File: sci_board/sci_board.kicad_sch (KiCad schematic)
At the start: 5 parts

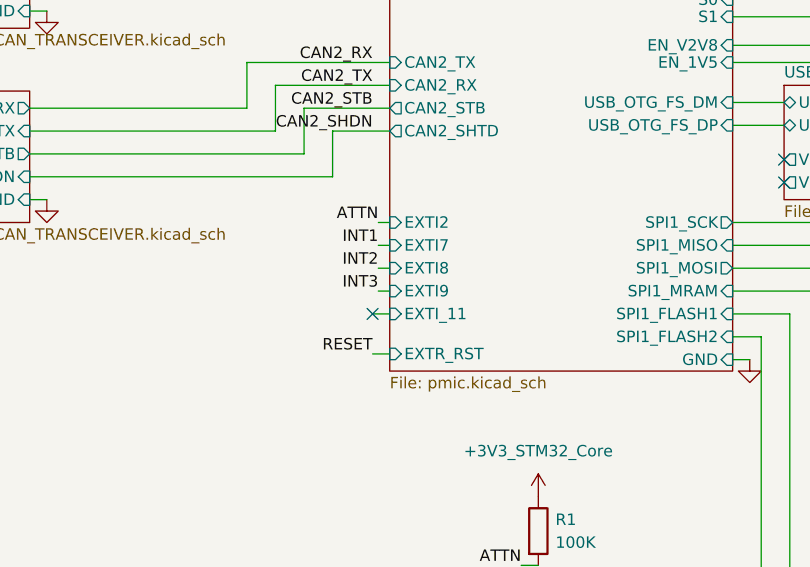
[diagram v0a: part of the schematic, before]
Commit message: add SPI CS and MISO pullups and terminations, remove WD from SCI
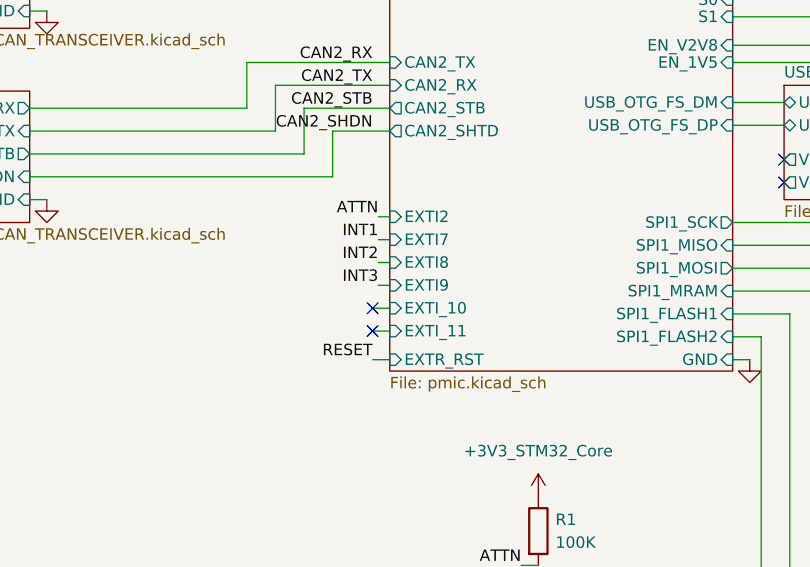
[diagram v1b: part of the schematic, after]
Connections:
- no-connect marks 37 -> 38
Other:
- sheet PMIC ports: added EXTI_10; removed none
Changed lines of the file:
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@@
 	)
 	(no_connect
+		(at 86.36 126.365)
+	)
+	(no_connect
 		(at 88.265 40.005)
 	)
 	(no_connect
-		(at 86.36 124.46)
+		(at 86.36 123.825)
 	)
 	(no_connect
@@
 	(wire
 		(pts
-			(xy 86.995 119.38) (xy 88.265 119.38)
+			(xy 86.995 118.745) (xy 88.265 118.745)
 		)
 		(stroke
@@
 	(wire
 		(pts
-			(xy 86.995 114.3) (xy 88.265 114.3)
+			(xy 86.995 113.665) (xy 88.265 113.665)
 		)
 		(stroke
@@
 	(wire
 		(pts
-			(xy 86.995 121.92) (xy 88.265 121.92)
+			(xy 86.995 121.285) (xy 88.265 121.285)
 		)
 		(stroke
@@
 	(wire
 		(pts
+			(xy 86.36 126.365) (xy 88.265 126.365)
+		)
+		(stroke
+			(width 0)
+			(type default)
+		)
+	)
+	(wire
+		(pts
 			(xy 48.26 88.265) (xy 88.265 88.265)
 		)
@@
 	(wire
 		(pts
-			(xy 86.36 124.46) (xy 88.265 124.46)
+			(xy 86.36 123.825) (xy 88.265 123.825)
 		)
 		(stroke
@@
 	(wire
 		(pts
-			(xy 86.36 128.905) (xy 88.265 128.905)
+			(xy 86.36 129.54) (xy 88.265 129.54)
 		)
 		(stroke
@@
 	(wire
 		(pts
-			(xy 86.995 116.84) (xy 88.265 116.84)
+			(xy 86.995 116.205) (xy 88.265 116.205)
 		)
 		(stroke
@@
 	)
 	(label "INT3"
-		(at 86.995 121.92 180)
+		(at 86.995 121.285 180)
 		(fields_autoplaced yes)
 		(effects
@@
 	)
 	(label "INT2"
-		(at 86.995 119.38 180)
+		(at 86.995 118.745 180)
 		(fields_autoplaced yes)
 		(effects
@@
 	)
 	(label "INT1"
-		(at 86.995 116.84 180)
+		(at 86.995 116.205 180)
 		(fields_autoplaced yes)
 		(effects
@@
 	)
 	(label "ATTN"
-		(at 86.995 114.3 180)
+		(at 86.995 113.665 180)
 		(fields_autoplaced yes)
 		(effects
@@
 	)
 	(label "RESET"
-		(at 86.36 128.905 180)
+		(at 86.36 129.54 180)
 		(fields_autoplaced yes)
 		(effects
@@
 		)
 		(pin "EXTI8" input
-			(at 88.265 119.38 180)
+			(at 88.265 118.745 180)
 			(effects
 				(font
@@
 		)
 		(pin "EXTI7" input
-			(at 88.265 116.84 180)
+			(at 88.265 116.205 180)
 			(effects
 				(font
@@
 		)
 		(pin "EXTI9" input
-			(at 88.265 121.92 180)
+			(at 88.265 121.285 180)
 			(effects
 				(font
@@
 		)
 		(pin "EXTR_RST" input
-			(at 88.265 128.905 180)
+			(at 88.265 129.54 180)
 			(effects
 				(font
@@
 		)
 		(pin "EXTI_11" input
-			(at 88.265 124.46 180)
+			(at 88.265 126.365 180)
 			(effects
 				(font
@@
 		)
 		(pin "EXTI2" input
-			(at 88.265 114.3 180)
+			(at 88.265 113.665 180)
 			(effects
 				(font
@@
 			(effects
 				(font
+					(size 1.27 1.27)
+				)
+				(justify left)
+			)
+		)
+		(pin "EXTI_10" input
+			(at 88.265 123.825 180)
+			(effects
+				(font

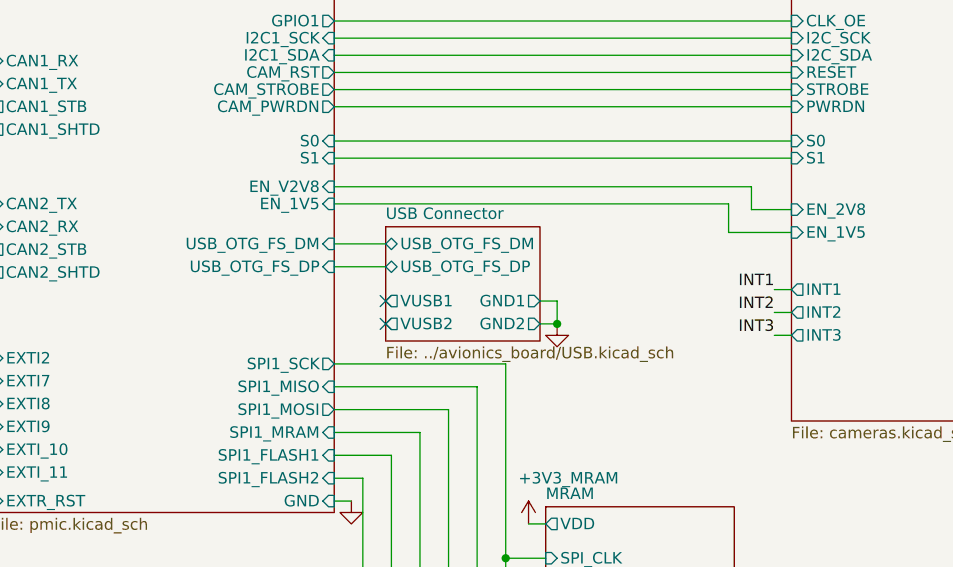
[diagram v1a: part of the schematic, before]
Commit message: tweaking SCI and AUX for production, using common sheets as much as possible
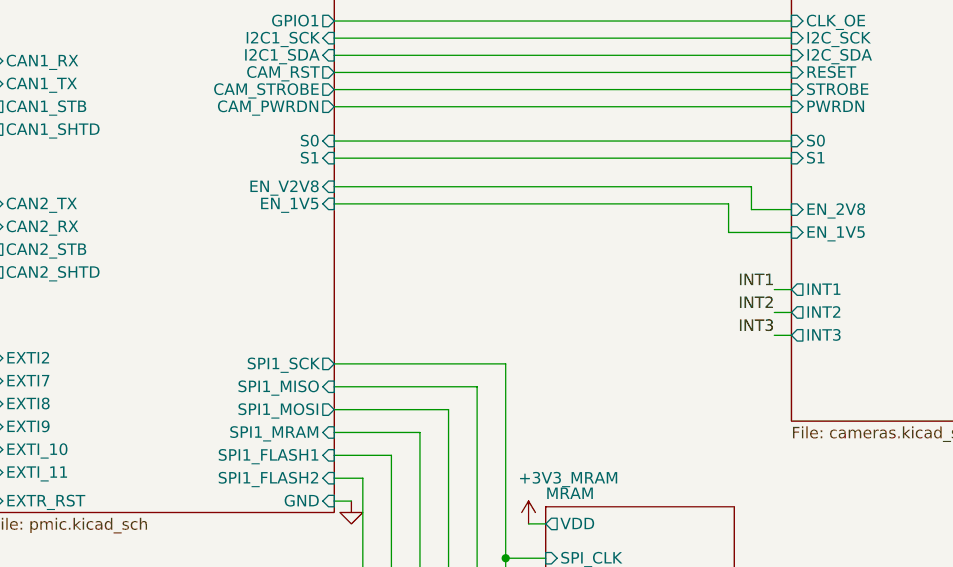
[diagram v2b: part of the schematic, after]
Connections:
- no-connect marks 38 -> 36
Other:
- removed sheet USB Connector
- sheet PMIC ports: added none; removed USB_OTG_FS_DM, USB_OTG_FS_DP
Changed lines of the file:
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@@
 	)
 	(junction
-		(at 151.13 109.855)
-		(diameter 0)
-		(color 0 0 0 0)
-	)
-	(junction
 		(at 142.24 138.43)
 		(diameter 0)
@@
 	)
 	(no_connect
-		(at 132.08 109.855)
-	)
-	(no_connect
 		(at 88.265 42.545)
 	)
@@
 	)
 	(no_connect
-		(at 132.08 107.315)
-	)
-	(no_connect
 		(at 266.7 47.625)
 	)
@@
 	(wire
 		(pts
-			(xy 149.225 107.315) (xy 151.13 107.315)
-		)
-		(stroke
-			(width 0)
-			(type default)
-		)
-	)
-	(wire
-		(pts
 			(xy 126.365 76.2) (xy 177.165 76.2)
 		)
@@
 	(wire
 		(pts
-			(xy 126.365 100.965) (xy 132.08 100.965)
-		)
-		(stroke
-			(width 0)
-			(type default)
-		)
-	)
-	(wire
-		(pts
 			(xy 139.065 165.735) (xy 149.86 165.735)
 		)
@@
 	(wire
 		(pts
-			(xy 149.225 109.855) (xy 151.13 109.855)
-		)
-		(stroke
-			(width 0)
-			(type default)
-		)
-	)
-	(wire
-		(pts
 			(xy 126.365 43.815) (xy 177.165 43.815)
 		)
@@
 	(wire
 		(pts
-			(xy 126.365 103.505) (xy 132.08 103.505)
-		)
-		(stroke
-			(width 0)
-			(type default)
-		)
-	)
-	(wire
-		(pts
 			(xy 22.225 90.805) (xy 24.765 90.805)
 		)
@@
 	(wire
 		(pts
-			(xy 151.13 107.315) (xy 151.13 109.855)
-		)
-		(stroke
-			(width 0)
-			(type default)
-		)
-	)
-	(wire
-		(pts
 			(xy 86.995 116.205) (xy 88.265 116.205)
 		)
@@
 		(dnp no)
 		(fields_autoplaced yes)
-		(property "Reference" "#PWR034"
+		(property "Reference" "#PWR033"
 			(at 174.625 198.12 0)
 			(effects
@@
 			(project "sci_board"
 				(path "/b4b2c88d-f6cd-4e60-862d-e21f68728580"
-					(reference "#PWR034")
+					(reference "#PWR033")
 					(unit 1)
 				)
@@
 		(dnp no)
 		(fields_autoplaced yes)
-		(property "Reference" "#PWR025"
+		(property "Reference" "#PWR024"
 			(at 213.995 125.095 0)
 			(effects
@@
 			(project "sci_board"
 				(path "/b4b2c88d-f6cd-4e60-862d-e21f68728580"
-					(reference "#PWR025")
+					(reference "#PWR024")
 					(unit 1)
 				)
@@
 	)
 	(symbol
-		(lib_id "power:GND")
-		(at 151.13 109.855 0)
-		(unit 1)
-		(exclude_from_sim no)
-		(in_bom yes)
-		(on_board yes)
-		(dnp no)
-		(fields_autoplaced yes)
-		(property "Reference" "#PWR023"
-			(at 151.13 116.205 0)
-			(effects
-				(font
-					(size 1.27 1.27)
-				)
-				(hide yes)
-			)
-		)
-		(property "Value" "GND"
-			(at 151.13 114.3 0)
-			(effects
-				(font
-					(size 1.27 1.27)
-				)
-				(hide yes)
-			)
-		)
-		(property "Footprint" ""
-			(at 151.13 109.855 0)
-			(effects
-				(font
-					(size 1.27 1.27)
-				)
-				(hide yes)
-			)
-		)
-		(property "Datasheet" ""
-			(at 151.13 109.855 0)
-			(effects
-				(font
-					(size 1.27 1.27)
-				)
-				(hide yes)
-			)
-		)
-		(property "Description" "Power symbol creates a global label with name \"GND\" , ground"
-			(at 151.13 109.855 0)
-			(effects
-				(font
-					(size 1.27 1.27)
-				)
-				(hide yes)
-			)
-		)
-		(pin "1"
-		)
-		(instances
-			(project "sci_board"
-				(path "/b4b2c88d-f6cd-4e60-862d-e21f68728580"
-					(reference "#PWR023")
-					(unit 1)
-				)
-			)
-		)
-	)
-	(symbol
 		(lib_id "power:PWR_FLAG")
 		(at 67.945 20.955 270)
@@
 		(dnp no)
 		(fields_autoplaced yes)
-		(property "Reference" "#PWR026"
+		(property "Reference" "#PWR025"
 			(at 128.27 135.89 0)
 			(effects
@@
 			(project "sci_board"
 				(path "/b4b2c88d-f6cd-4e60-862d-e21f68728580"
-					(reference "#PWR026")
+					(reference "#PWR025")
 					(unit 1)
 				)
@@
 		(on_board yes)
 		(dnp no)
-		(property "Reference" "#PWR027"
+		(property "Reference" "#PWR026"
 			(at 147.955 135.89 0)
 			(effects
@@
 			(project "sci_board"
 				(path "/b4b2c88d-f6cd-4e60-862d-e21f68728580"
-					(reference "#PWR027")
+					(reference "#PWR026")
 					(unit 1)
 				)
@@
 		(dnp no)
 		(fields_autoplaced yes)
-		(property "Reference" "#PWR024"
+		(property "Reference" "#PWR023"
 			(at 50.165 118.11 0)
 			(effects
@@
 			(project "sci_board"
 				(path "/b4b2c88d-f6cd-4e60-862d-e21f68728580"
-					(reference "#PWR024")
+					(reference "#PWR023")
 					(unit 1)
 				)
@@
 		(dnp no)
 		(fields_autoplaced yes)
-		(property "Reference" "#PWR029"
+		(property "Reference" "#PWR028"
 			(at 173.99 151.13 0)
 			(effects
@@
 			(project "sci_board"
 				(path "/b4b2c88d-f6cd-4e60-862d-e21f68728580"
-					(reference "#PWR029")
+					(reference "#PWR028")
 					(unit 1)
 				)
@@
 		(dnp no)
 		(fields_autoplaced yes)
-		(property "Reference" "#PWR031"
+		(property "Reference" "#PWR030"
 			(at 275.59 168.91 0)
 			(effects
@@
 			(project "sci_board"
 				(path "/b4b2c88d-f6cd-4e60-862d-e21f68728580"
-					(reference "#PWR031")
+					(reference "#PWR030")
 					(unit 1)
 				)
@@
 		(dnp no)
 		(fields_autoplaced yes)
-		(property "Reference" "#PWR032"
+		(property "Reference" "#PWR031"
 			(at 174.625 174.625 0)
 			(effects
@@
 			(project "sci_board"
 				(path "/b4b2c88d-f6cd-4e60-862d-e21f68728580"
-					(reference "#PWR032")
+					(reference "#PWR031")
 					(unit 1)
 				)
@@
 		(on_board yes)
 		(dnp no)
-		(property "Reference" "#PWR033"
+		(property "Reference" "#PWR032"
 			(at 147.32 184.15 0)
 			(effects
@@
 			(project "sci_board"
 				(path "/b4b2c88d-f6cd-4e60-862d-e21f68728580"
-					(reference "#PWR033")
+					(reference "#PWR032")
 					(unit 1)
 				)
@@
 		(on_board yes)
 		(dnp no)
-		(property "Reference" "#PWR030"
+		(property "Reference" "#PWR029"
 			(at 147.32 160.655 0)
 			(effects
@@
 			(project "sci_board"
 				(path "/b4b2c88d-f6cd-4e60-862d-e21f68728580"
-					(reference "#PWR030")
+					(reference "#PWR029")
 					(unit 1)
 				)
@@
 		(dnp no)
 		(fields_autoplaced yes)
-		(property "Reference" "#PWR028"
+		(property "Reference" "#PWR027"
 			(at 104.775 148.59 0)
 			(effects
@@
 			(project "sci_board"
 				(path "/b4b2c88d-f6cd-4e60-862d-e21f68728580"
-					(reference "#PWR028")
+					(reference "#PWR027")
 					(unit 1)
 				)
@@
 			)
 		)
-		(pin "USB_OTG_FS_DM" input
-			(at 126.365 100.965 0)
-			(effects
-				(font
-					(size 1.27 1.27)
-				)
-				(justify right)
-			)
-		)
-		(pin "USB_OTG_FS_DP" input
-			(at 126.365 103.505 0)
-			(effects
-				(font
-					(size 1.27 1.27)
-				)
-				(justify right)
-			)
-		)
 		(pin "DCMI_02" input
 			(at 126.365 49.53 0)
@@
 				)
 			)
-		)
-	)
-	(sheet
-		(at 132.08 99.06)
-		(size 17.145 12.7)
-		(fields_autoplaced yes)
-		(stroke
-			(width 0.1524)
-			(type solid)
-		)
-		(fill
-			(color 0 0 0 0.0000)
-		)
-		(property "Sheetname" "USB Connector"
-			(at 132.08 98.3484 0)
-			(effects
-				(font
-					(size 1.27 1.27)
-				)
-				(justify left bottom)
-			)
-		)
-		(property "Sheetfile" "../avionics_board/USB.kicad_sch"
-			(at 132.08 112.3446 0)
-			(effects
-				(font
-					(size 1.27 1.27)
-				)
-				(justify left top)
-			)
-		)
-		(pin "GND1" output
-			(at 149.225 107.315 0)
-			(effects
-				(font
-					(size 1.27 1.27)
-				)
-				(justify right)
-			)
-		)
-		(pin "USB_OTG_FS_DM" bidirectional
-			(at 132.08 100.965 180)
-			(effects
-				(font
-					(size 1.27 1.27)
-				)
-				(justify left)
-			)
-		)
-		(pin "VUSB1" output
-			(at 132.08 107.315 180)
-			(effects
-				(font
-					(size 1.27 1.27)
-				)
-				(justify left)
-			)
-		)
-		(pin "GND2" output
-			(at 149.225 109.855 0)
-			(effects
-				(font
-					(size 1.27 1.27)
-				)
-				(justify right)
-			)
-		)
-		(pin "VUSB2" output
-			(at 132.08 109.855 180)
-			(effects
-				(font
-					(size 1.27 1.27)
-				)
-				(justify left)
-			)
-		)
-		(pin "USB_OTG_FS_DP" bidirectional
-			(at 132.08 103.505 180)
-			(effects
-				(font
-					(size 1.27 1.27)
-				)
-				(justify left)
-			)
-		)
-		(instances
-			(project "sci_board"
-				(path "/b4b2c88d-f6cd-4e60-862d-e21f68728580"
-					(page "15")
-				)
-			)

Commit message: clenup BOM for SCI and AUX
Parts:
- R1: value 100K -> 330K
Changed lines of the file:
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@@
 			)
 		)
-		(property "Value" "100K"
+		(property "Value" "330K"
 			(at 106.68 149.8599 0)
 			(effects

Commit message: cleaning up bom: remove main camera port since it has not pullups and capacitors, correcting some errors in camera switch
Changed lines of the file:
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@@
+	)
+	(symbol
+		(lib_id "power:GND")
+		(at 141.605 19.05 0)
+		(mirror y)
+		(unit 1)
+		(exclude_from_sim no)
+		(in_bom yes)
+		(on_board yes)
+		(dnp no)
+		(fields_autoplaced yes)
+		(property "Reference" "#PWR02"
+			(at 141.605 25.4 0)
+			(effects
+				(font
+					(size 1.27 1.27)
+				)
+				(hide yes)
+			)
+		)
+		(property "Value" "GND"
+			(at 141.605 23.495 0)
+			(effects
+				(font
+					(size 1.27 1.27)
+				)
+				(hide yes)
+			)
+		)
+		(property "Footprint" ""
+			(at 141.605 19.05 0)
+			(effects
+				(font
+					(size 1.27 1.27)
+				)
+				(hide yes)
+			)
+		)
+		(property "Datasheet" ""
+			(at 141.605 19.05 0)
+			(effects
+				(font
+					(size 1.27 1.27)
+				)
+				(hide yes)
+			)
+		)
+		(property "Description" "Power symbol creates a global label with name \"GND\" , ground"
+			(at 141.605 19.05 0)
+			(effects
+				(font
+					(size 1.27 1.27)
+				)
+				(hide yes)
+			)
+		)
+		(pin "1"
+		)
+		(instances
+			(project "sci_board"
+				(path "/b4b2c88d-f6cd-4e60-862d-e21f68728580"
+					(reference "#PWR02")
+					(unit 1)
+				)
+			)
+		)
 	)
 	(symbol
@@
 	)
 	(symbol
+		(lib_id "power:PWR_FLAG")
+		(at 141.605 19.05 270)
+		(unit 1)
+		(exclude_from_sim no)
+		(in_bom yes)
+		(on_board yes)
+		(dnp no)
+		(fields_autoplaced yes)
+		(property "Reference" "#FLG02"
+			(at 143.51 19.05 0)
+			(effects
+				(font
+					(size 1.27 1.27)
+				)
+				(hide yes)
+			)
+		)
+		(property "Value" "PWR_FLAG"
+			(at 144.78 19.0499 90)
+			(effects
+				(font
+					(size 1.27 1.27)
+				)
+				(justify left)
+			)
+		)
+		(property "Footprint" ""
+			(at 141.605 19.05 0)
+			(effects
+				(font
+					(size 1.27 1.27)
+				)
+				(hide yes)
+			)
+		)
+		(property "Datasheet" "~"
+			(at 141.605 19.05 0)
+			(effects
+				(font
+					(size 1.27 1.27)
+				)
+				(hide yes)
+			)
+		)
+		(property "Description" "Special symbol for telling ERC where power comes from"
+			(at 141.605 19.05 0)
+			(effects
+				(font
+					(size 1.27 1.27)
+				)
+				(hide yes)
+			)
+		)
+		(pin "1"
+		)
+		(instances
+			(project "sci_board"
+				(path "/b4b2c88d-f6cd-4e60-862d-e21f68728580"
+					(reference "#FLG02")
+					(unit 1)
+				)
+			)
+		)
+	)
+	(symbol
 		(lib_id "power:GND")
 		(at 53.975 56.515 0)
@@
 				(path "/b4b2c88d-f6cd-4e60-862d-e21f68728580"
 					(reference "#PWR025")
-					(unit 1)
-				)
-			)
-		)
-	)
-	(symbol
-		(lib_id "power:PWR_FLAG")
-		(at 134.62 18.415 270)
-		(unit 1)
-		(exclude_from_sim no)
-		(in_bom yes)
-		(on_board yes)
-		(dnp no)
-		(fields_autoplaced yes)
-		(property "Reference" "#FLG02"
-			(at 136.525 18.415 0)
-			(effects
-				(font
-					(size 1.27 1.27)
-				)
-				(hide yes)
-			)
-		)
-		(property "Value" "PWR_FLAG"
-			(at 137.795 18.4149 90)
-			(effects
-				(font
-					(size 1.27 1.27)
-				)
-				(justify left)
-			)
-		)
-		(property "Footprint" ""
-			(at 134.62 18.415 0)
-			(effects
-				(font
-					(size 1.27 1.27)
-				)
-				(hide yes)
-			)
-		)
-		(property "Datasheet" "~"
-			(at 134.62 18.415 0)
-			(effects
-				(font
-					(size 1.27 1.27)
-				)
-				(hide yes)
-			)
-		)
-		(property "Description" "Special symbol for telling ERC where power comes from"
-			(at 134.62 18.415 0)
-			(effects
-				(font
-					(size 1.27 1.27)
-				)
-				(hide yes)
-			)
-		)
-		(pin "1"
-		)
-		(instances
-			(project "sci_board"
-				(path "/b4b2c88d-f6cd-4e60-862d-e21f68728580"
-					(reference "#FLG02")
 					(unit 1)
 				)
@@
 					(unit 1)
 				)
-			)
-		)
-	)
-	(symbol
-		(lib_id "power:GND")
-		(at 134.62 18.415 0)
-		(mirror y)
-		(unit 1)
-		(exclude_from_sim no)
-		(in_bom yes)
-		(on_board yes)
-		(dnp no)
-		(fields_autoplaced yes)
-		(property "Reference" "#PWR02"
-			(at 134.62 24.765 0)
-			(effects
-				(font
-					(size 1.27 1.27)
-				)
-				(hide yes)
-			)
-		)
-		(property "Value" "GND"
-			(at 134.62 22.86 0)
-			(effects
-				(font
-					(size 1.27 1.27)
-				)
-				(hide yes)
-			)
-		)
-		(property "Footprint" ""
-			(at 134.62 18.415 0)
-			(effects
-				(font
-					(size 1.27 1.27)
-				)
-				(hide yes)
-			)
-		)
-		(property "Datasheet" ""
-			(at 134.62 18.415 0)
-			(effects
-				(font
-					(size 1.27 1.27)
-				)
-				(hide yes)
-			)
-		)
-		(property "Description" "Power symbol creates a global label with name \"GND\" , ground"
-			(at 134.62 18.415 0)
-			(effects
-				(font
-					(size 1.27 1.27)
-				)
-				(hide yes)
-			)
-		)
-		(pin "1"
-		)
-		(instances
-			(project "sci_board"
-				(path "/b4b2c88d-f6cd-4e60-862d-e21f68728580"
-					(reference "#PWR02")
-					(unit 1)
-				)

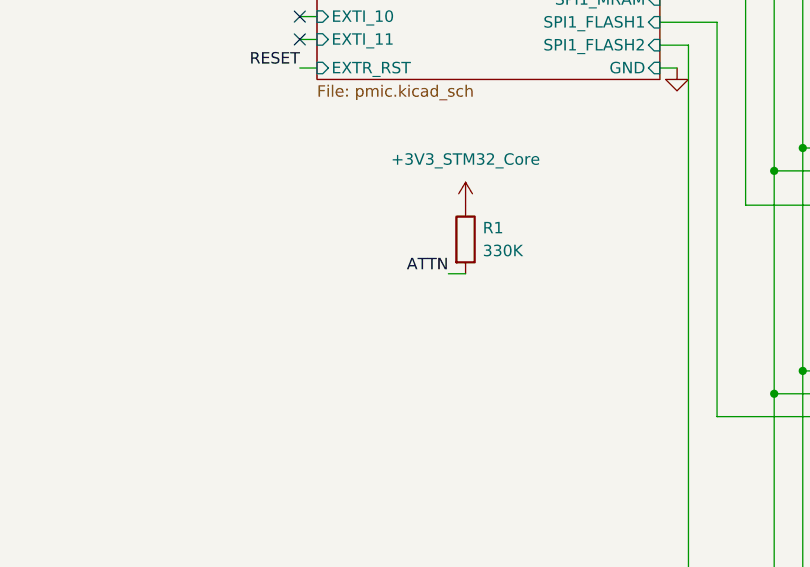
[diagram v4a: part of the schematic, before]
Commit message: QC, add second 3V regulator to AUX, INT pullups on AUX SCI AVI
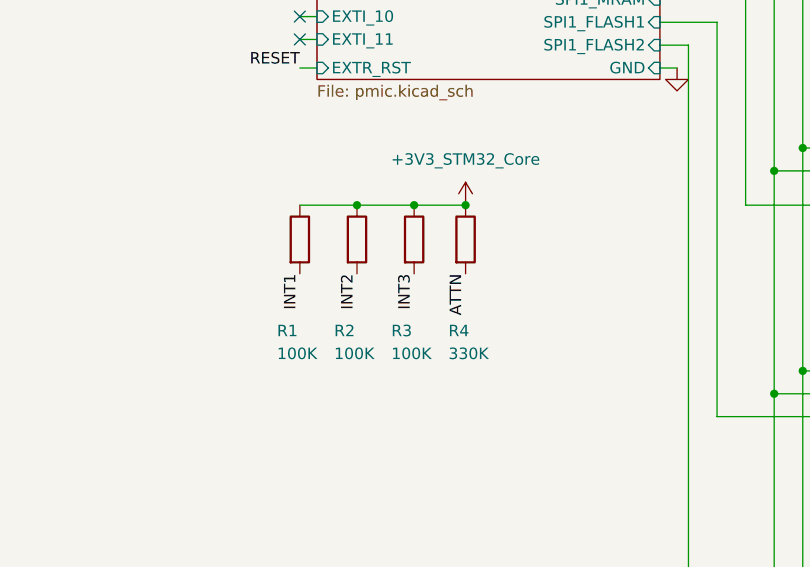
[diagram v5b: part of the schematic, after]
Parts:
- added R1, R2, R3: 100K, Resistor_SMD:R_0402_1005Metric_Pad0.72x0.64mm_HandSolder, symbol Device:R
- renumbered R1 to R4
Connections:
- net +3V3_STM32_Core: now also R1.1, R2.1, R3.1
- net INT1: now also R1.2
- net INT2: now also R2.2
- net INT3: now also R3.2
